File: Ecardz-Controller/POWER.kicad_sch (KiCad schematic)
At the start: 2 parts, among them J1 Conn_01x02, J2 Conn_01x04_Pin

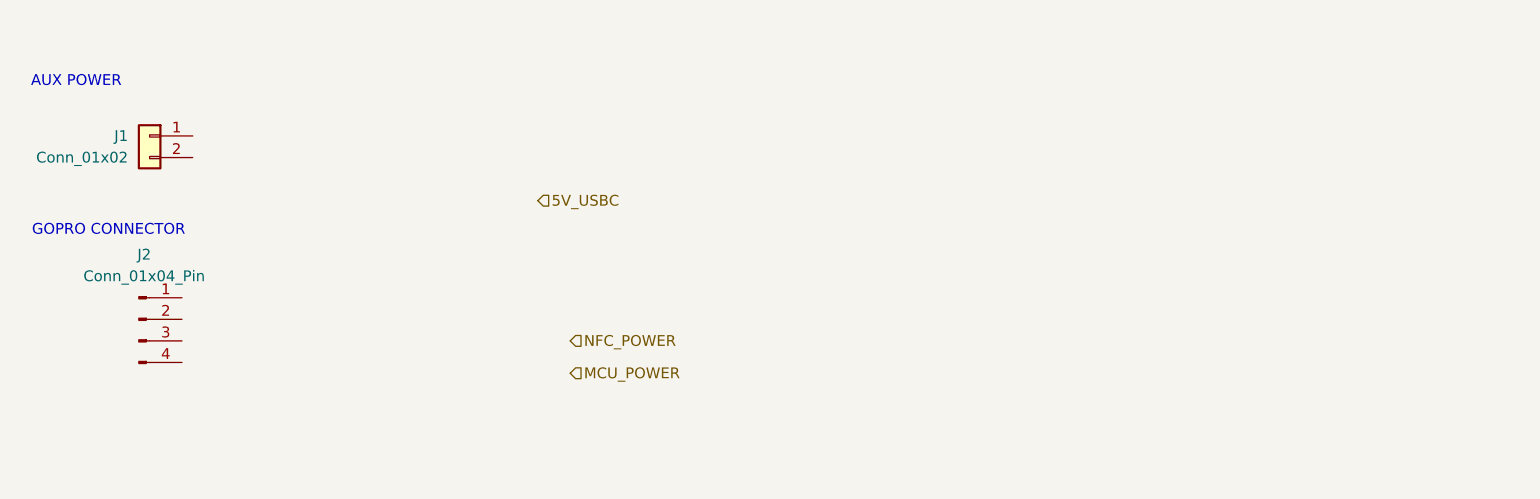
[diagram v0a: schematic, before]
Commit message: added buck converter
just missing inductor part selection
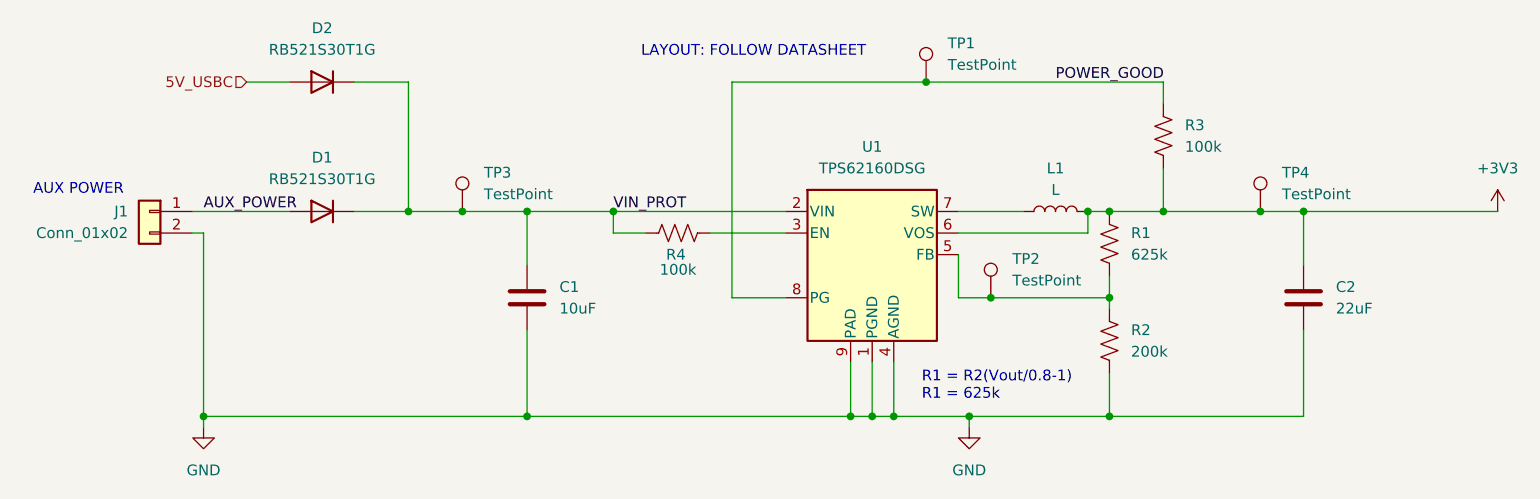
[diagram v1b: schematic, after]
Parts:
- removed J2: Conn_01x04_Pin, symbol Connector:Conn_01x04_Pin
- added C1: 10uF, Capacitor_SMD:C_0805_2012Metric_Pad1.18x1.45mm_HandSolder, symbol Device:C
- added C2: 22uF, Capacitor_SMD:C_0805_2012Metric_Pad1.18x1.45mm_HandSolder, symbol Device:C
- added D1, D2: RB521S30T1G, Diode_SMD:D_SOD-523, symbol Device:D
- added L1: L, symbol Device:L
- added R1: 625k, symbol Device:R_US
- added R2: 200k, symbol Device:R_US
- added R3, R4: 100k, symbol Device:R_US
- added TP1, TP2, TP3, TP4: TestPoint, TestPoint:TestPoint_Pad_D3.0mm, symbol Connector:TestPoint
- added U1: TPS62160DSG, Package_SON:WSON-8-1EP_2x2mm_P0.5mm_EP0.9x1.6mm_ThermalVias, symbol Regulator_Switching:TPS62160DSG
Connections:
- net 5V_USBC: now also D2.2 (A)
- net AUX_POWER: now reaches J1.1 (Pin_1)
- net AUX_POWER: now also D1.2 (A)
- net GND: now reaches J1.2 (Pin_2)
- net GND: now also C1.2, C2.2, R2.2, U1.1 (PGND), U1.4 (AGND), U1.9 (PAD)
- new net: R4.1, U1.3 (EN)
- new net: R1.2, R2.1, TP2.1, U1.5 (FB)
- new net: L1.1, U1.7 (SW)
- new net +3V3: C2.1, L1.2, R1.1, R3.2, TP4.1, U1.6 (VOS)
- new net POWER_GOOD: R3.1, TP1.1, U1.8 (PG)
- new net VIN_PROT: C1.1, D1.1 (K), D2.1 (K), R4.2, TP3.1, U1.2 (VIN)
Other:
- note added: "LAYOUT: FOLLOW DATASHEET"
- note added: "R1 = R2(Vout/0.8-1) R1 = 625k"
- note removed: "GOPRO CONNECTOR"
- moved on the sheet: J1

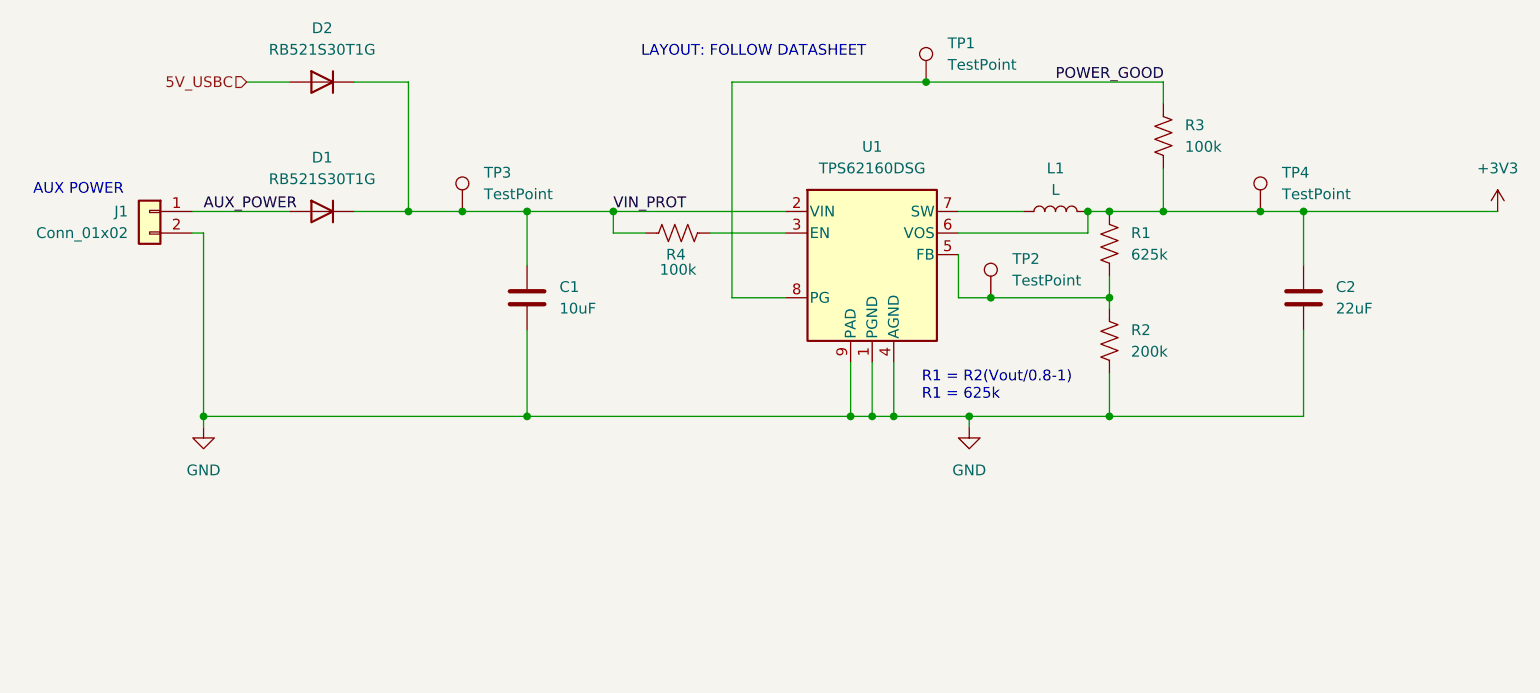
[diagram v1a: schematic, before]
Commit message: adding MCU
added peripheral connections as well as indicator lights
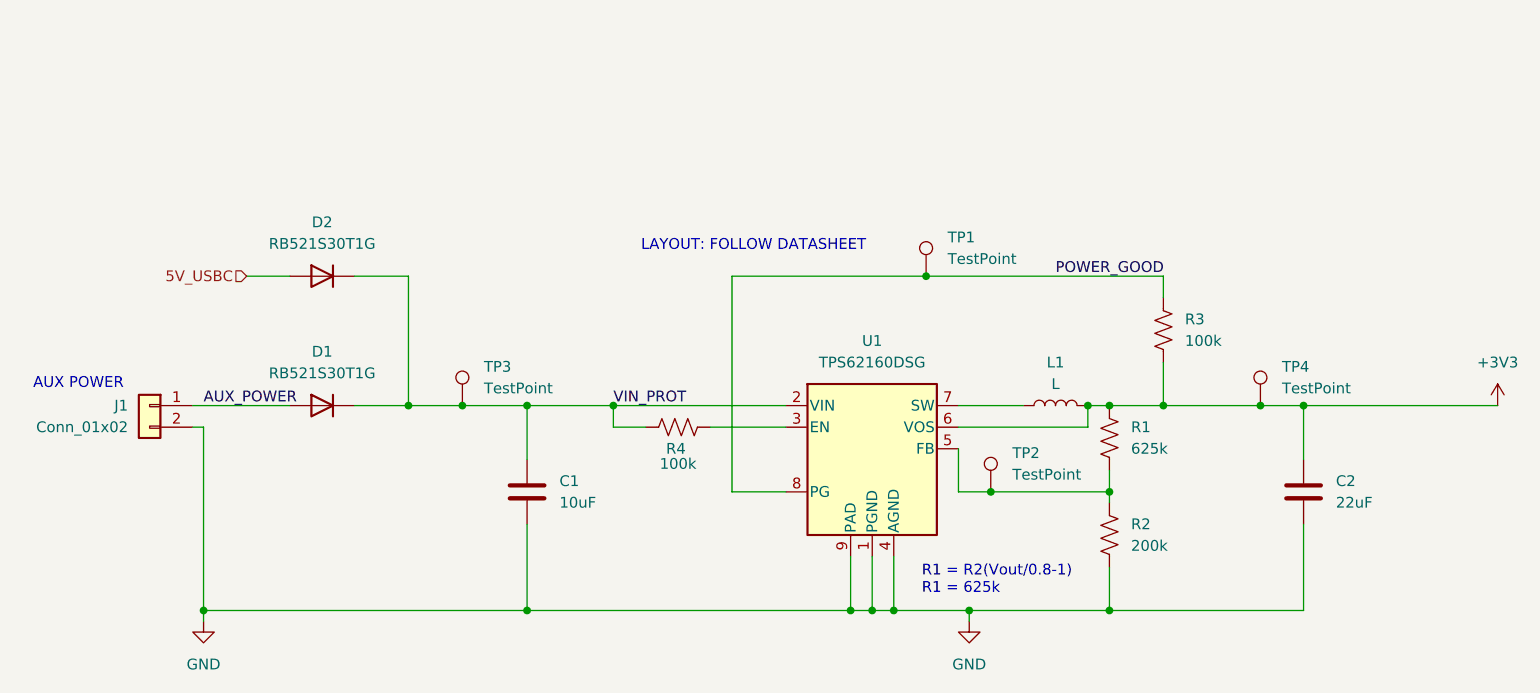
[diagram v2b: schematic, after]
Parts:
- U1: Part Number (none) -> TPS62160DSG
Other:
- moved on the sheet: C1, C2, D1, D2, J1, L1, R1, R2, R3, R4, TP1, TP2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

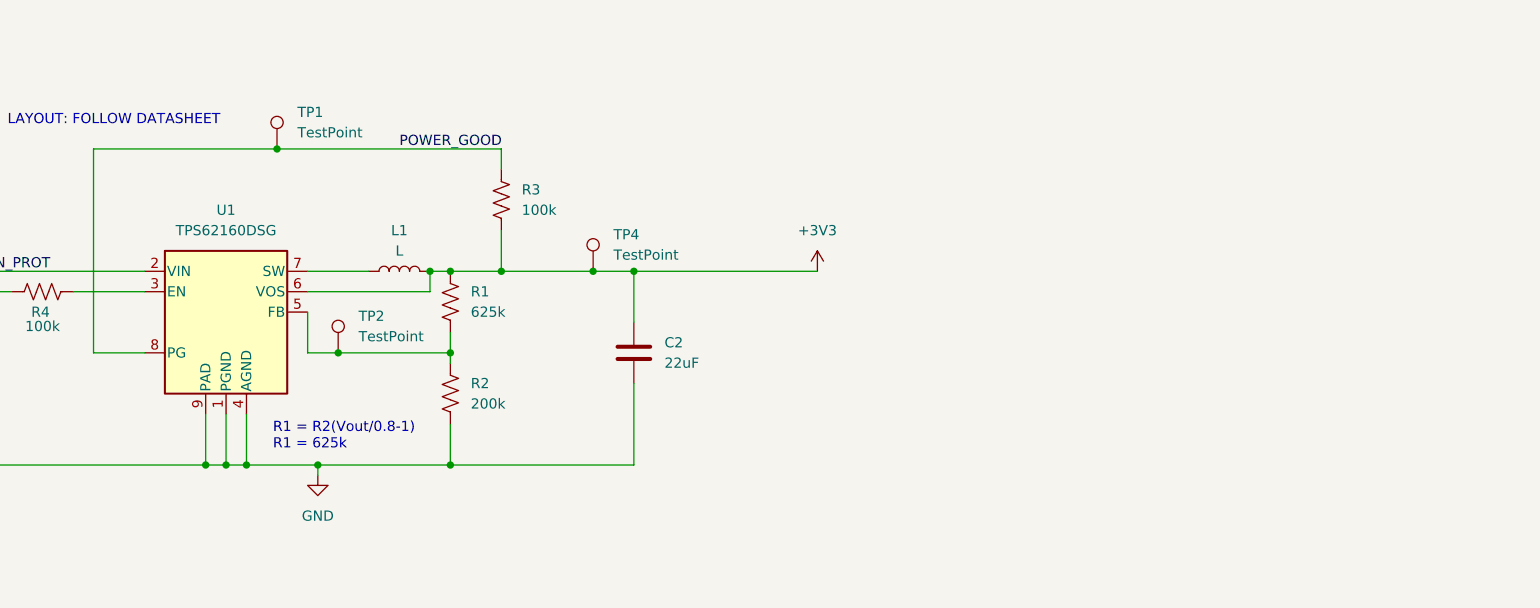
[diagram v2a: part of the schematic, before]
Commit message: added LDO on buck output and SD card footprint
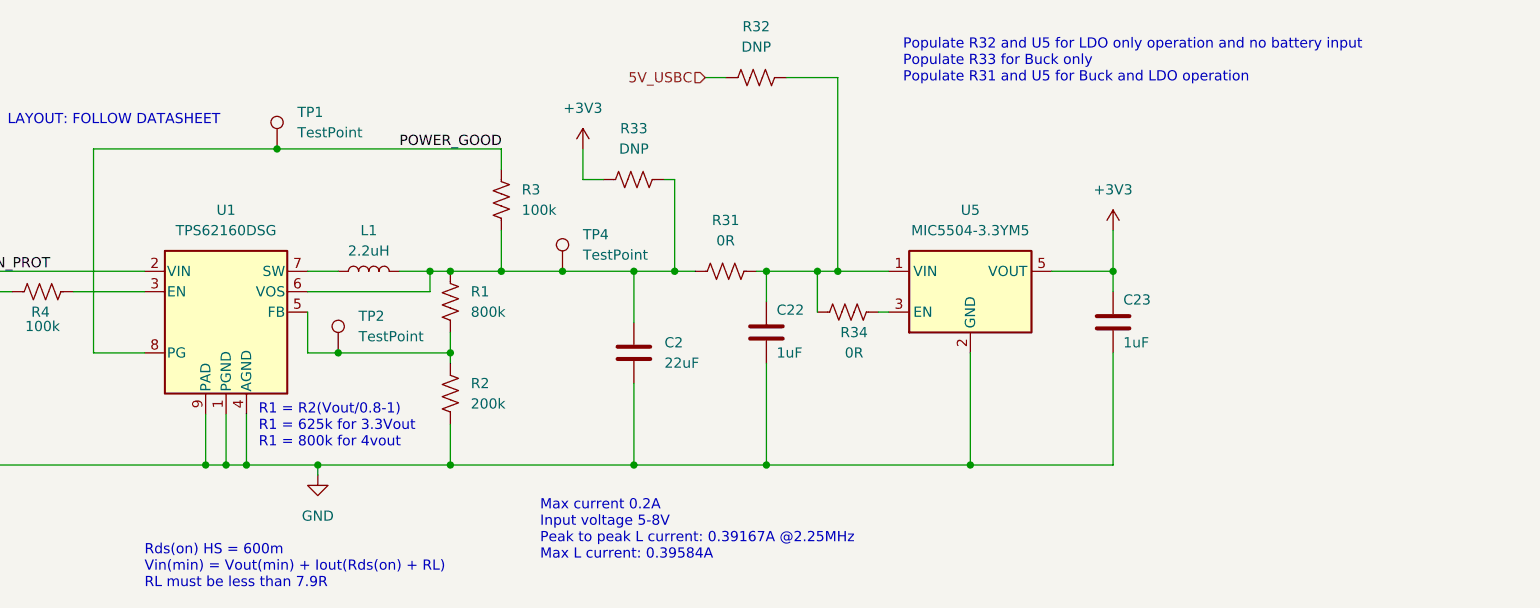
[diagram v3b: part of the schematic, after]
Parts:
- added C22, C23: 1uF, Capacitor_SMD:C_0603_1608Metric_Pad1.08x0.95mm_HandSolder, symbol Device:C
- added R31, R34: 0R, Resistor_SMD:R_0603_1608Metric_Pad0.98x0.95mm_HandSolder, symbol Device:R_US
- added R32, R33: DNP, Resistor_SMD:R_0603_1608Metric_Pad0.98x0.95mm_HandSolder, symbol Device:R_US
- added U5: MIC5504-3.3YM5, Package_TO_SOT_SMD:SOT-23-5, symbol Regulator_Linear:MIC5504-3.3YM5
- L1: value L -> 2.2uH; footprint (none) -> SamacSys_Parts:VLS2016; Part Number (none) -> VLS201610CX-2R2M-1
- R1: value 625k -> 800k; footprint (none) -> Resistor_SMD:R_0603_1608Metric_Pad0.98x0.95mm_HandSolder; Part Number (none) -> ERJ-3EKF7873V
- R2: footprint (none) -> Resistor_SMD:R_0603_1608Metric_Pad0.98x0.95mm_HandSolder; Part Number (none) -> RC0603JR-07200KL
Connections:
- net +3V3: now also C23.1, R33.1, U5.5 (VOUT); no longer C2.1, L1.2, R1.1, R3.2, TP4.1, U1.6 (VOS)
- net 5V_USBC: now also R32.1
- net GND: now also C22.2, C23.2, U5.2 (GND)
- new net: R34.1, U5.3 (EN)
- new net: C22.1, R31.2, R32.2, R34.2, U5.1 (VIN)
- new net: C2.1, L1.2, R1.1, R3.2, R31.1, R33.2, TP4.1, U1.6 (VOS)
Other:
- note added: "Max current 0.2A Input voltage 5-8V Peak to peak L current: 0.39167A @2.25MHz Max L current: 0.39584A"
- note added: "Populate R32 and U5 for LDO only operation and no battery input Populate R33 for Buck only Populate R31 and U5 for Buck and LDO operation"
- note added: "R1 = R2(Vout/0.8-1) R1 = 625k for 3.3Vout R1 = 800k for 4vout"
- note added: "Rds(on) HS = 600m Vin(min) = Vout(min) + Iout(Rds(on) + RL) RL must be less than 7.9R"
- note removed: "R1 = R2(Vout/0.8-1) R1 = 625k"
- moved on the sheet: L1, TP4
